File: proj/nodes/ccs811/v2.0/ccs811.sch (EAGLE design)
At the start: 1 part

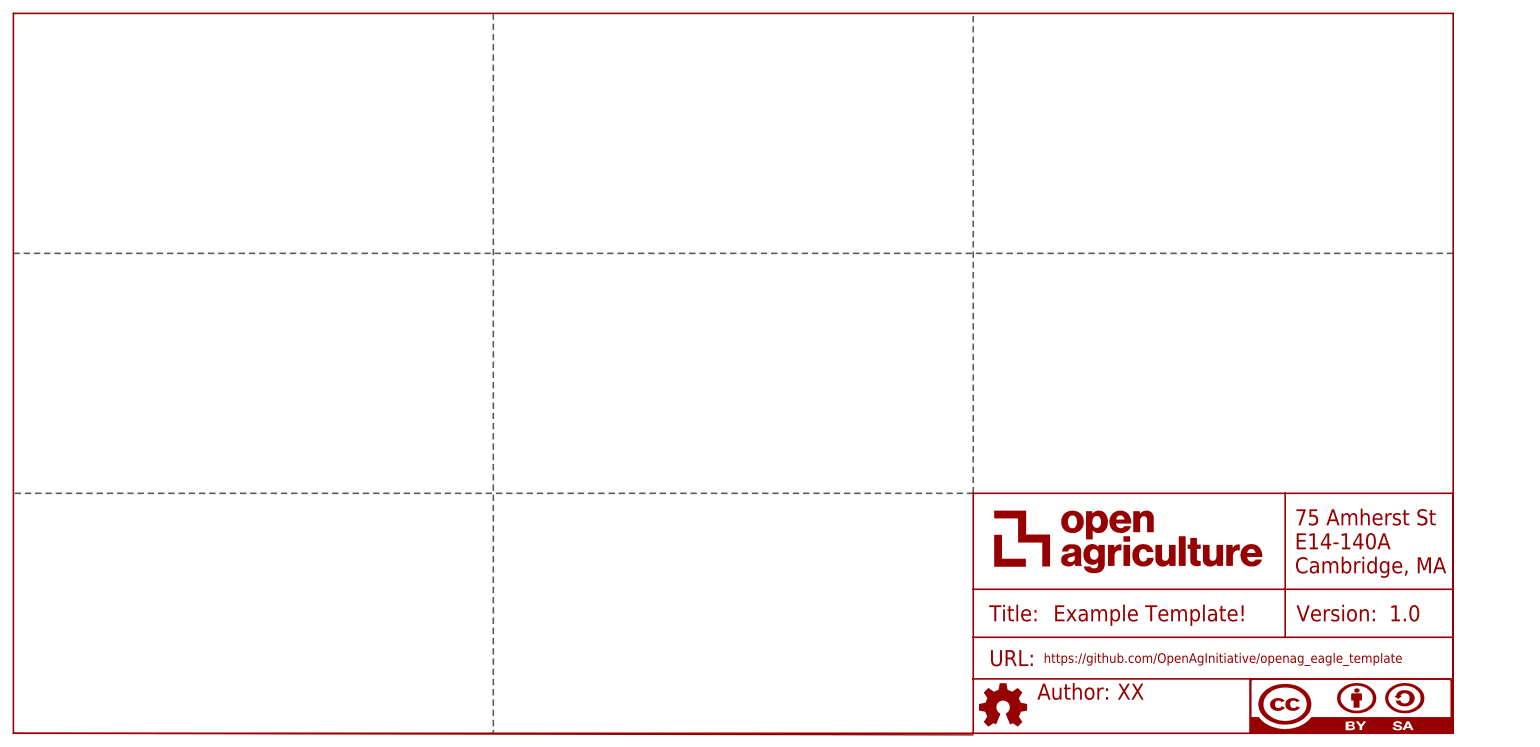
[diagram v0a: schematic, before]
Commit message: cleaned up design blocks, added co2 sensor node v2.0
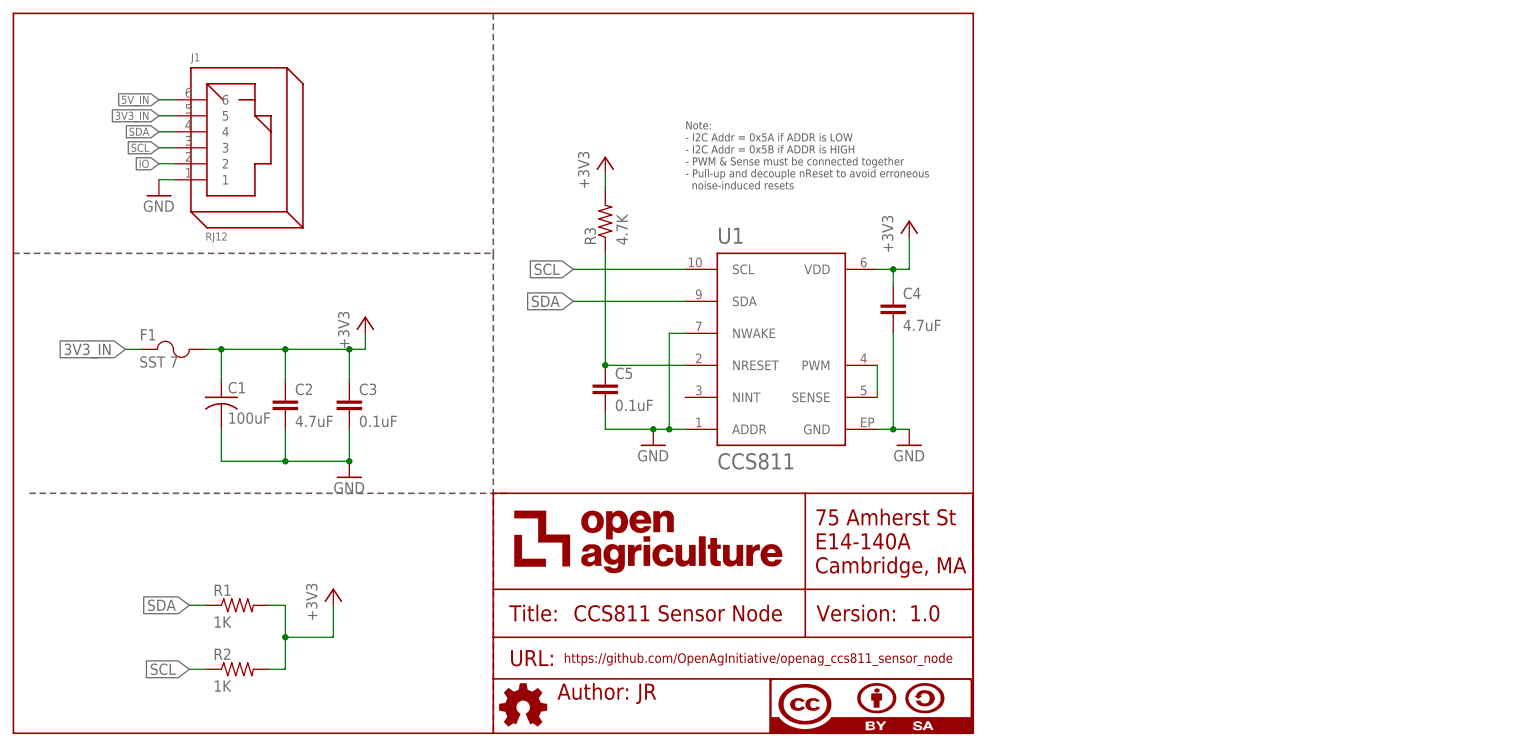
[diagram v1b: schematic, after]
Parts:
- added C1: 100uF, openag-capacitors:100UF-EEE-1HA101UP
- added C2, C4: 4.7uF, openag-capacitors:4.7UF-CL21A475KBQNNNE
- added C3, C5: 0.1uF, openag-capacitors:0.1UF-C0603C104K5RACTU
- added F1: SST 7, openag-fuses:SST_7
- added J1: RJ12, openag-connectors:A-2004-1-4-LP-N-R
- added R1, R2: 1K, openag-resistors:1K-ERJ-PB3D1001V
- added R3: 4.7K, openag-resistors:4.7K-RC1206JR-074K7L
- added U1: CCS811, openag-sensors:CCS811
- FRAME1: AUTHOR (none) -> JR; DESCRIPTION (none) -> CCS811 CO2 Sensor Node; TITLE Example Template! -> CCS811 Sensor Node; URL (none) -> https://github.com/OpenAgInitiative/openag_ccs811_sensor_no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
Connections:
- new net +3V3: C1.1(+), C2.1, C3.1, C4.1, F1.2, R1.2, R2.2, R3.2, U1.VDD
- new net 3V3_IN: F1.1, J1.5
- new net 5V_IN: J1.6
- new net GND: C1.2(-), C2.2, C3.2, C4.2, C5.2, J1.1, U1.ADDR, U1.GND, U1.NWAKE
- new net IO: J1.2
- new net N$4: U1.PWM, U1.SENSE
- new net N$5: C5.1, R3.1, U1.NRESET
- new net SCL: J1.3, R2.1, U1.SCL
- new net SDA: J1.4, R1.1, U1.SDA
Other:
- note added: "CCS811 CO2 Sensor"
- note added: "I2C Pullup Resistors"
- note added: "Note: - I2C Addr = 0x5A if ADDR is LOW - I2C Addr = 0x5B if ADDR is HIGH - PWM & Sense must be connected together - Pull-up and decouple nReset to avoid erroneous noise-induced resets"
- note added: "Power Conditioning"
- note added: "RJ12 Connector"
